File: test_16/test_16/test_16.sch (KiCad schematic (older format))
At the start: 81 parts, among them J1 Array set 0, J2 Array set 0

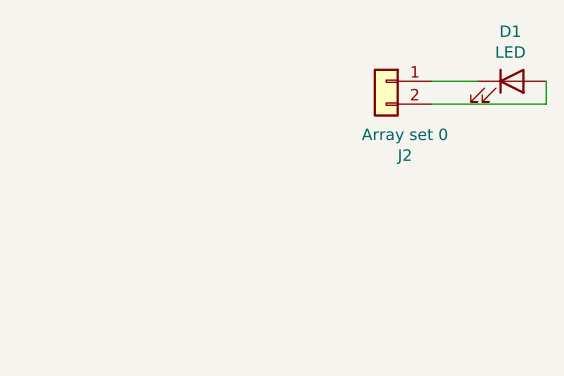
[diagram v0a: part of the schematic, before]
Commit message: bracket alignement
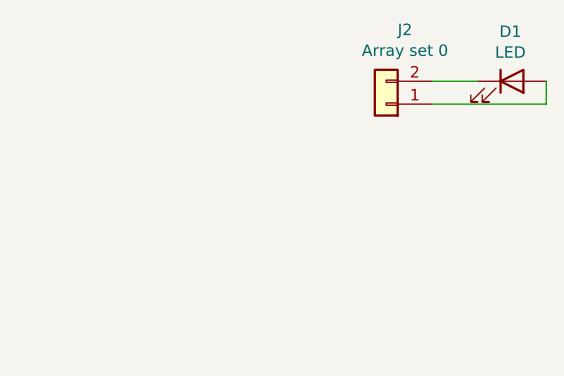
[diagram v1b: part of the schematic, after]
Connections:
- net at D1.1 (K): now also J2.2 (Pin_2); no longer J2.1 (Pin_1)
- net at D1.2 (A): now also J2.1 (Pin_1); no longer J2.2 (Pin_2)
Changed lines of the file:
@@
 L Connector_Generic:Conn_01x02 J2
 U 1 1 6107F170
-P 8950 900
-F 0 "J2" H 8868 575 50  0000 C CNN
-F 1 "Array set 0" H 8868 666 50  0000 C CNN
-F 2 "Connector_Phoenix_MC:PhoenixContact_MCV_1,5_2-G-3.5_1x02_P3.50mm_Vertical" H 8950 900 50  0001 C CNN
-F 3 "~" H 8950 900 50  0001 C CNN
-	1    8950 900
-	-1   0    0    -1
+P 8950 1000
+F 0 "J2" H 8868 675 50  0000 C CNN
+F 1 "Array set 0" H 8868 766 50  0000 C CNN
+F 2 "Connector_Phoenix_MC:PhoenixContact_MCV_1,5_2-G-3.5_1x02_P3.50mm_Vertical" H 8950 1000 50  0001 C CNN
+F 3 "~" H 8950 1000 50  0001 C CNN
+	1    8950 1000
+	-1   0    0    1
 $EndComp
 Wire Wire Line
